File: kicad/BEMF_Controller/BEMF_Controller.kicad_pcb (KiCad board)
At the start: 2 copper layers, 201.8 x 175 mm, 228 parts, among them J1 HEADER4VALULOK, J2 HEADER6, J3 FUSE, J4 HEADER6, J5 Load, J7 Vin, Q1 C3M0280090D, Q11 C3M0280090D, Q2 C3M0280090D, Q3 C3M0280090D, Q4 C3M0280090D, Q5 C3M0280090D, Q6 C3M0280090D, Q7 C3M0280090D, Q9 C3M0280090D, U1 Raspberry Pi Pico, U10 OPA2376AIDR, U11 ADC108S022CIMTX/NOPB, U12 OPA2376AIDR, U13 INA181, U14 INA181, U15 INA181, U16 OPA2376AIDR, U18 ISO7760FQDWRQ1, U19 DGD2304, U2 INA181, U20 DGD2304, U21 DGD2304, U3 V_REG_78XX, U4 TC1240A, U5 DGD2304, U6 DGD2304, U7 DGD2304, U8 ISO7760FQDWRQ1, U9 ISO7760FQDWRQ1

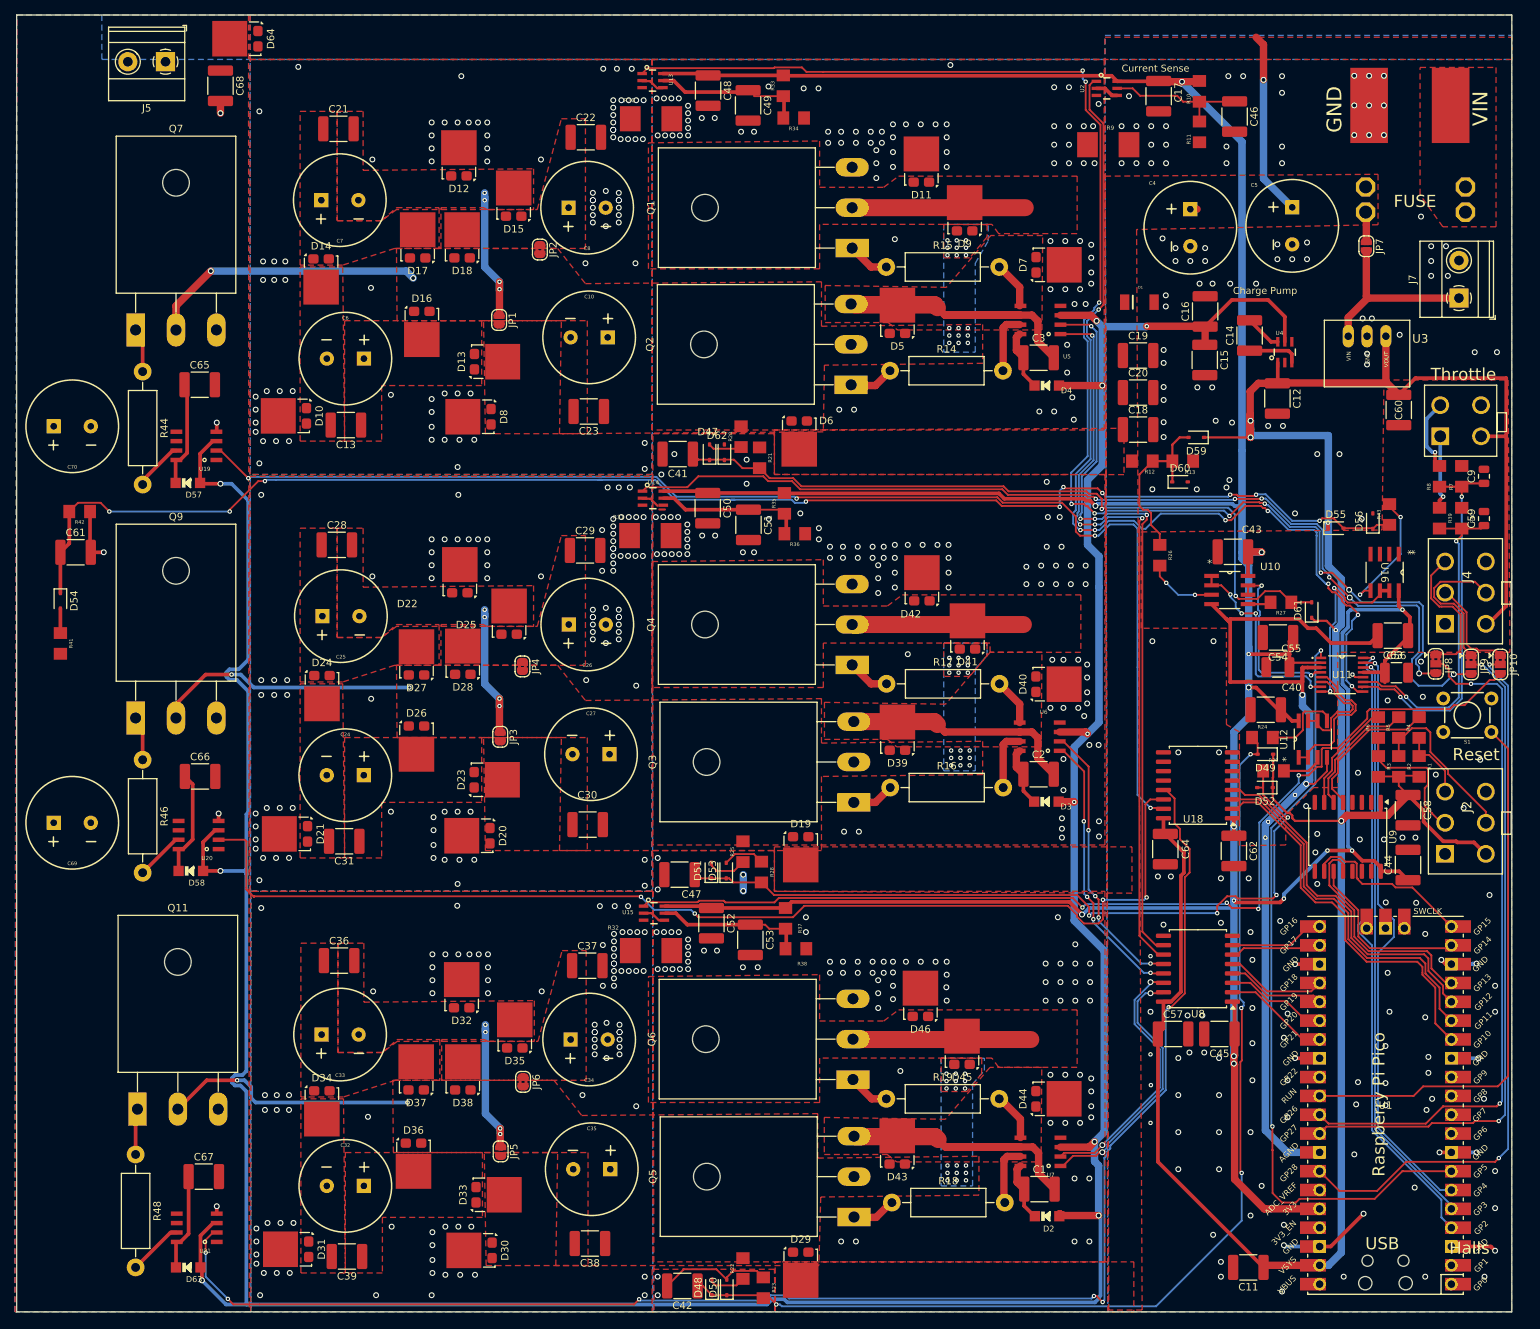
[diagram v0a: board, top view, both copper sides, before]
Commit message: Added analog Hall inputs and worked away lot of warnings.
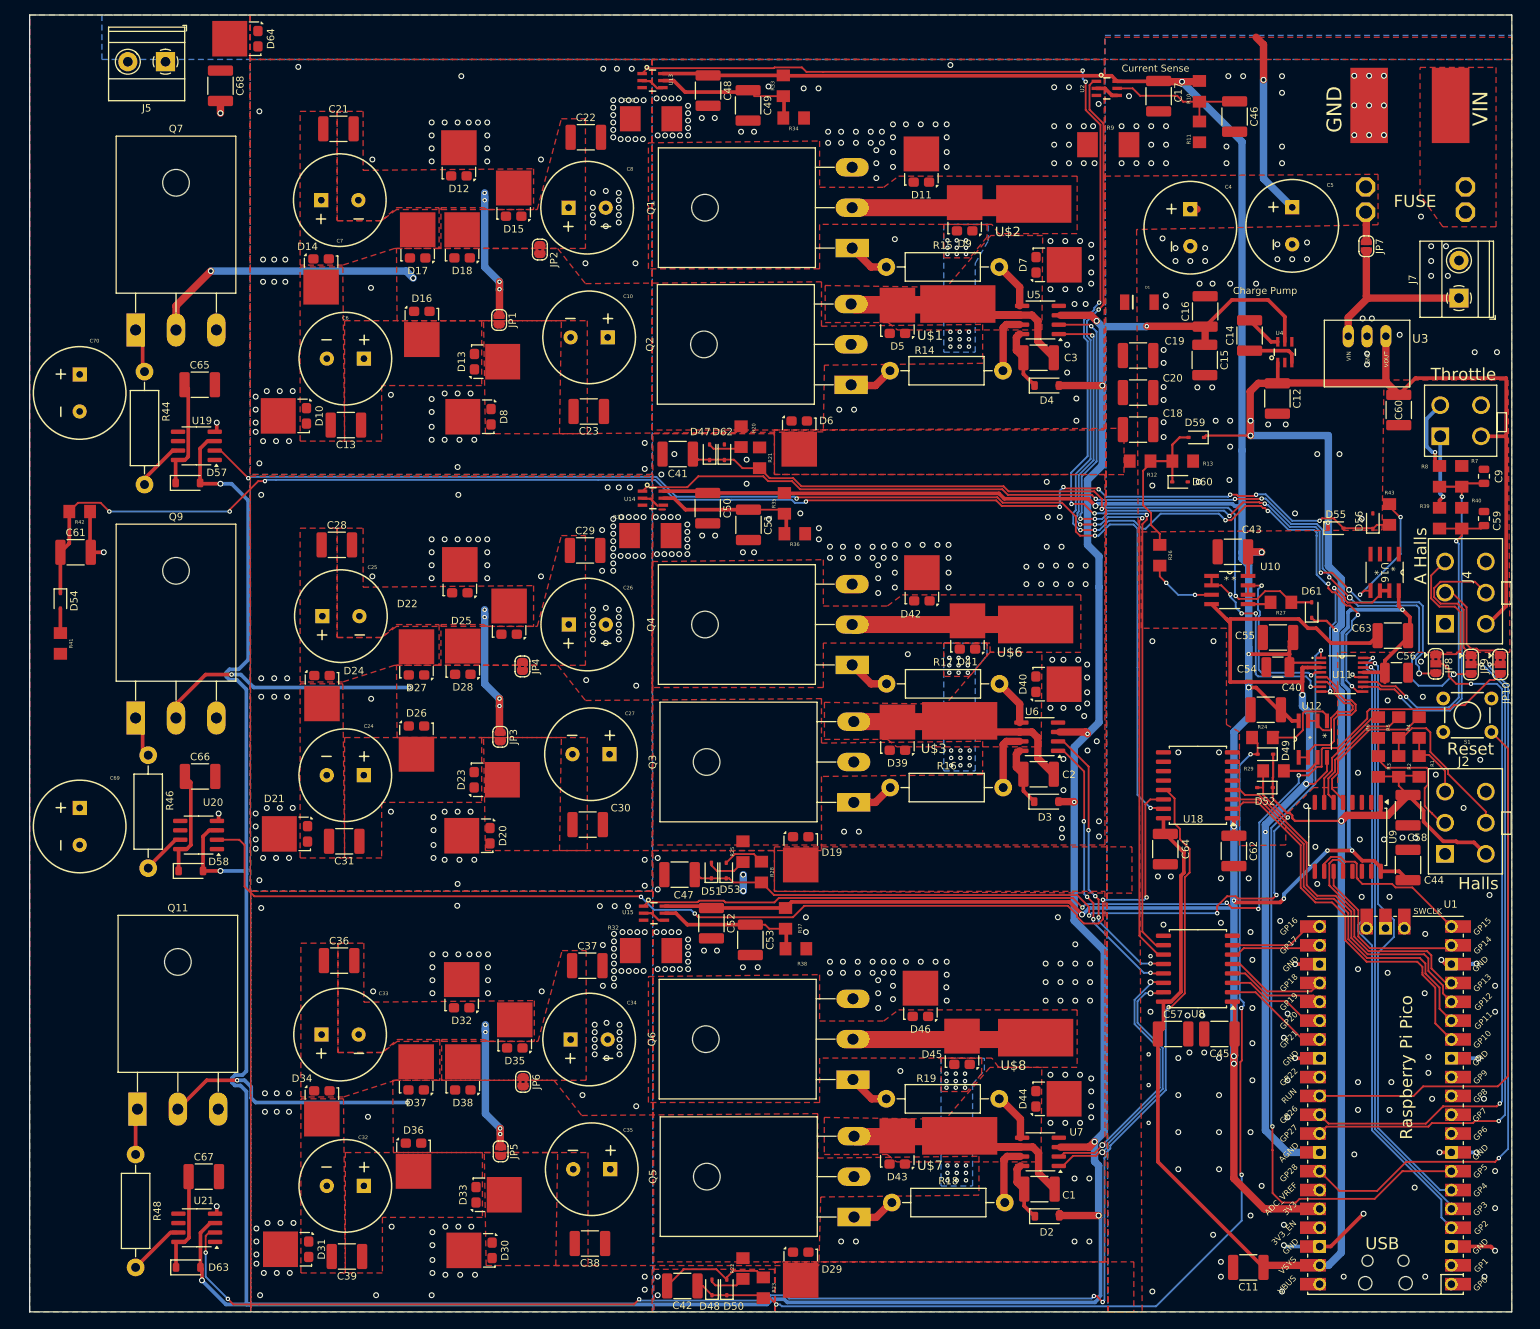
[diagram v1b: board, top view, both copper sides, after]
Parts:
- added U$1: PAD, main:PAD, F.Cu at (234.0, 92.8)
- added U$2: PAD, main:PAD, F.Cu at (244.2, 79.2)
- added U$3: PAD, main:PAD, F.Cu at (234.2, 149.0)
- added U$6: PAD, main:PAD, F.Cu at (244.5, 136.0)
- added U$7: PAD, main:PAD, F.Cu at (234.2, 205.0)
- added U$8: PAD, main:PAD, F.Cu at (244.5, 191.8)
- D2, D3, D4, D57, D58, D63: footprint main:SOD-123 -> Diode_SMD:D_SOD-123
- U19, U20, U21, U5, U6, U7: footprint main:SOIC8 -> Package_SO:SOIC-8_3.9x4.9mm_P1.27mm
- moved C70 4.61 mm to (115.5, 104.8), turned to 90 degrees
- moved C69 1.12 mm to (115.5, 163.2), turned to 90 degrees
- moved R46 0.97 mm to (124.8, 153.6)
- moved R12 0.30 mm to (258.6, 114.0)
- moved R44 0.25 mm to (124.2, 101.9)
- turned D2 to 0 degrees
- turned D3 to 0 degrees
- turned D4 to 0 degrees
- turned D57 to 0 degrees
- turned D58 to 0 degrees
- turned D63 to 0 degrees
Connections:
- C1 pad 1: Net-(U7-VB) -> Net-(D2-K)
- C2 pad 1: Net-(U6-VB) -> Net-(D3-K)
- C3 pad 1: Net-(U5-VB) -> Net-(D4-K)
- C65 pad 1: Net-(U19-VB) -> Net-(D57-K)
- C66 pad 1: Net-(U20-VB) -> Net-(D58-K)
- C67 pad 1: Net-(U21-VB) -> Net-(D63-K)
- U19 pad 8: Net-(U19-VB) -> Net-(D57-K)
- U20 pad 8: Net-(U20-VB) -> Net-(D58-K)
- U21 pad 8: Net-(U21-VB) -> Net-(D63-K)
- U5 pad 8: Net-(U5-VB) -> Net-(D4-K)
- U6 pad 8: Net-(U6-VB) -> Net-(D3-K)
- U7 pad 8: Net-(U7-VB) -> Net-(D2-K)
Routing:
- net Net-(D57-K): track 0.00 -> 14.8 mm
- net Net-(D58-K): track 0.00 -> 14.4 mm
- net Net-(U19-VB): track 14.3 -> 0.00 mm
- net Net-(U20-VB): track 14.3 -> 0.00 mm
- net Net-(D63-K): track 0.00 -> 13.6 mm
- net Net-(U21-VB): track 13.2 -> 0.00 mm
- net Net-(U7-VB): track 8.04 -> 0.00 mm
- net Net-(U6-VB): track 8.04 -> 0.00 mm
- net Net-(D3-K): track 0.00 -> 8.04 mm
- net Net-(D2-K): track 0.00 -> 8.04 mm
- net Net-(U5-VB): track 8.04 -> 0.00 mm
- net Net-(D4-K): track 0.00 -> 8.04 mm
- net 5V: track 364.0 -> 359.1 mm
- net 3.3V: track 527.7 -> 526.2 mm
- net /DCH_B_H: track 6.69 -> 5.76 mm
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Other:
- board size 201.8 x 175 mm -> 200 x 175 mm
- board text added: "A Halls"

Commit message: Simplification, high and low side driven together.
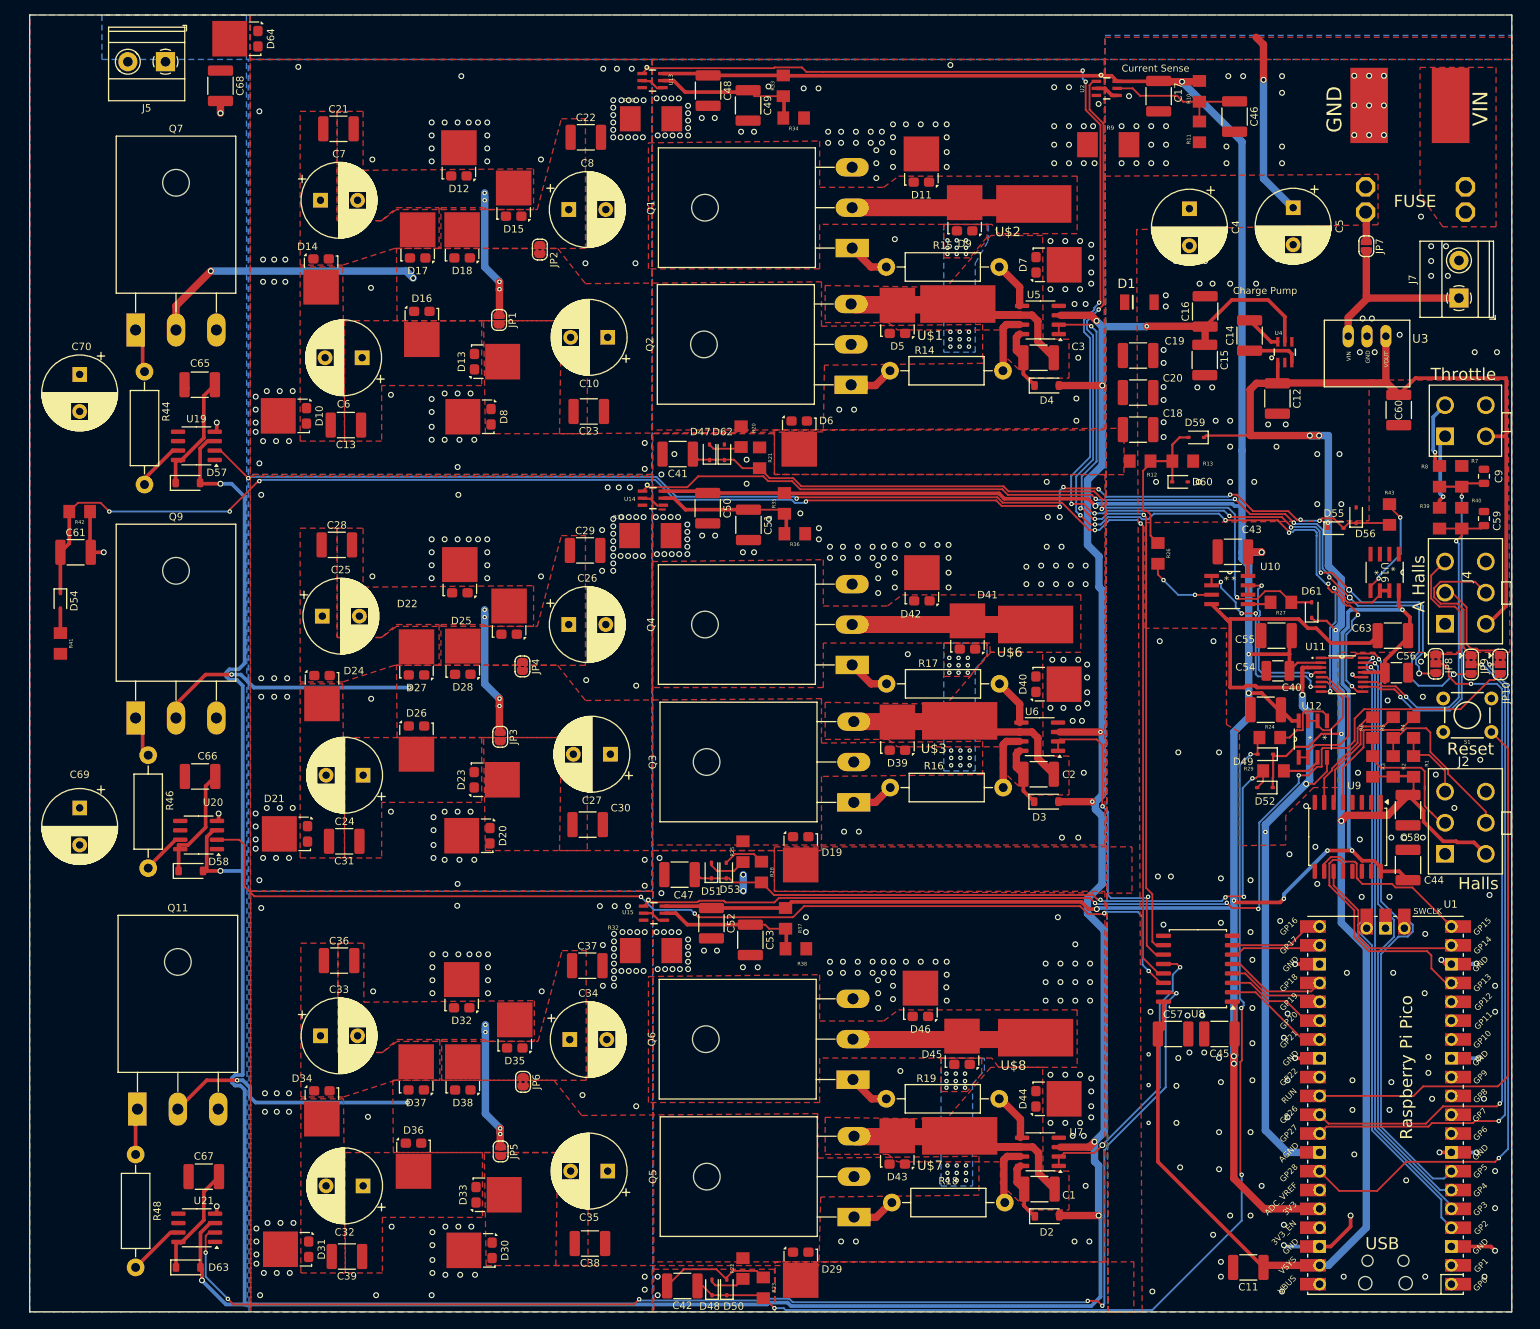
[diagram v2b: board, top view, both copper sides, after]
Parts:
- removed C62, C64: 1uF, Capacitor_SMD:C_1812_4532Metric
- removed U18: ISO7760FQDWRQ1, Package_SO:SOIC-16W_7.5x10.3mm_P1.27mm
- C10, C24, C25, C26, C27, C32, C33, C34, C35, C4, C5, C6, C69, C7, C70, C8: footprint main:CPOL-RADIAL-5MM-10MM -> Capacitor_THT:CP_Radial_D10.0mm_P5.00mm
- U$1: value PAD -> COIL_A+
- moved C33 2.65 mm to (148.0, 191.5), turned to 0 degrees
- moved C27 2.62 mm to (187.1, 153.5), turned to 180 degrees
- moved C34 2.62 mm to (181.6, 192.0), turned to 0 degrees
- moved C7 2.60 mm to (148.0, 78.8), turned to 0 degrees
- moved C4 2.57 mm to (265.2, 79.9), turned to -90 degrees
- moved C10 2.50 mm to (186.8, 97.2), turned to 180 degrees
- moved C25 2.50 mm to (148.2, 134.9), turned to 0 degrees
- moved C26 2.50 mm to (181.5, 136.0), turned to 0 degrees
- moved C69 2.50 mm to (115.5, 160.8), turned to -90 degrees
- moved C70 2.50 mm to (115.5, 102.2), turned to -90 degrees
- moved C8 2.49 mm to (181.5, 80.0), turned to 0 degrees
- moved C5 2.45 mm to (279.2, 79.8), turned to -90 degrees
- moved C24 2.41 mm to (153.8, 156.3), turned to 180 degrees
- moved C32 2.40 mm to (153.8, 211.8), turned to 180 degrees
- moved D56 2.39 mm to (287.8, 121.2)
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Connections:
- net /AH_O renamed /A_O
- net /AL_O renamed /B_O
- net /BH_O renamed /C_O
- U1 pad 14: /DA_O -> unconnected-(U1-GPIO10-Pad14)
- U1 pad 15: /DB_O -> unconnected-(U1-GPIO11-Pad15)
- U1 pad 16: /DC_O -> unconnected-(U1-GPIO12-Pad16)
- U1 pad 25: /BL_O -> /DA_O
- U1 pad 26: /CH_O -> /DB_O
- U1 pad 27: /CL_O -> /DC_O
- U1 pad 42: unconnected-(U1-GND-Pad42) -> GND
- U5 pad 1: /CTRL_AL -> /CTRL_A
- U5 pad 2: /CTRL_AH -> /CTRL_A
- U6 pad 1: /CTRL_BL -> /CTRL_B
- U6 pad 2: /CTRL_BH -> /CTRL_B
- U7 pad 1: /CTRL_CL -> /CTRL_C
- U7 pad 2: /CTRL_CH -> /CTRL_C
- U8 pad 10: /CTRL_AH -> /CTRL_A
- U8 pad 11: /CTRL_AL -> /CTRL_B
- U8 pad 12: /CTRL_BH -> /CTRL_C
- U8 pad 13: /CTRL_BL -> /CTRL_DA
- U8 pad 14: /CTRL_CH -> /CTRL_DB
- U8 pad 15: /CTRL_CL -> /CTRL_DC
- U8 pad 2: /CL_O -> /DC_O
- U8 pad 3: /CH_O -> /DB_O
- U8 pad 4: /BL_O -> /DA_O
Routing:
- net /CTRL_AH: track 100.8 -> 0.00 mm, vias 4 -> 0
- net /CTRL_AL: track 100.8 -> 0.00 mm, vias 4 -> 0
- net /CTRL_A: track 0.00 -> 100.5 mm, vias 0 -> 4
- net /CTRL_B: track 0.00 -> 43.3 mm, vias 0 -> 2
- net /DA_O: track 51.9 -> 13.4 mm
- net /CTRL_C: track 0.00 -> 38.4 mm, vias 0 -> 2
- net /CTRL_BH: track 37.9 -> 0.00 mm, vias 4 -> 0
- net /CTRL_BL: track 37.7 -> 0.00 mm, vias 4 -> 0
- net /DB_O: track 49.8 -> 13.9 mm
- net /CTRL_CH: track 35.6 -> 0.00 mm, vias 2 -> 0
- net /CTRL_CL: track 35.6 -> 0.00 mm, vias 2 -> 0
- net /DC_O: track 48.4 -> 14.4 mm
- net /CTRL_DC: track 206.9 -> 179.0 mm
- net /CTRL_DA: track 171.6 -> 192.6 mm
- net 5V: track 359.1 -> 343.0 mm, vias 5 -> 6
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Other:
- board text added: "DUTY"

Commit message: Fixed all warnings.
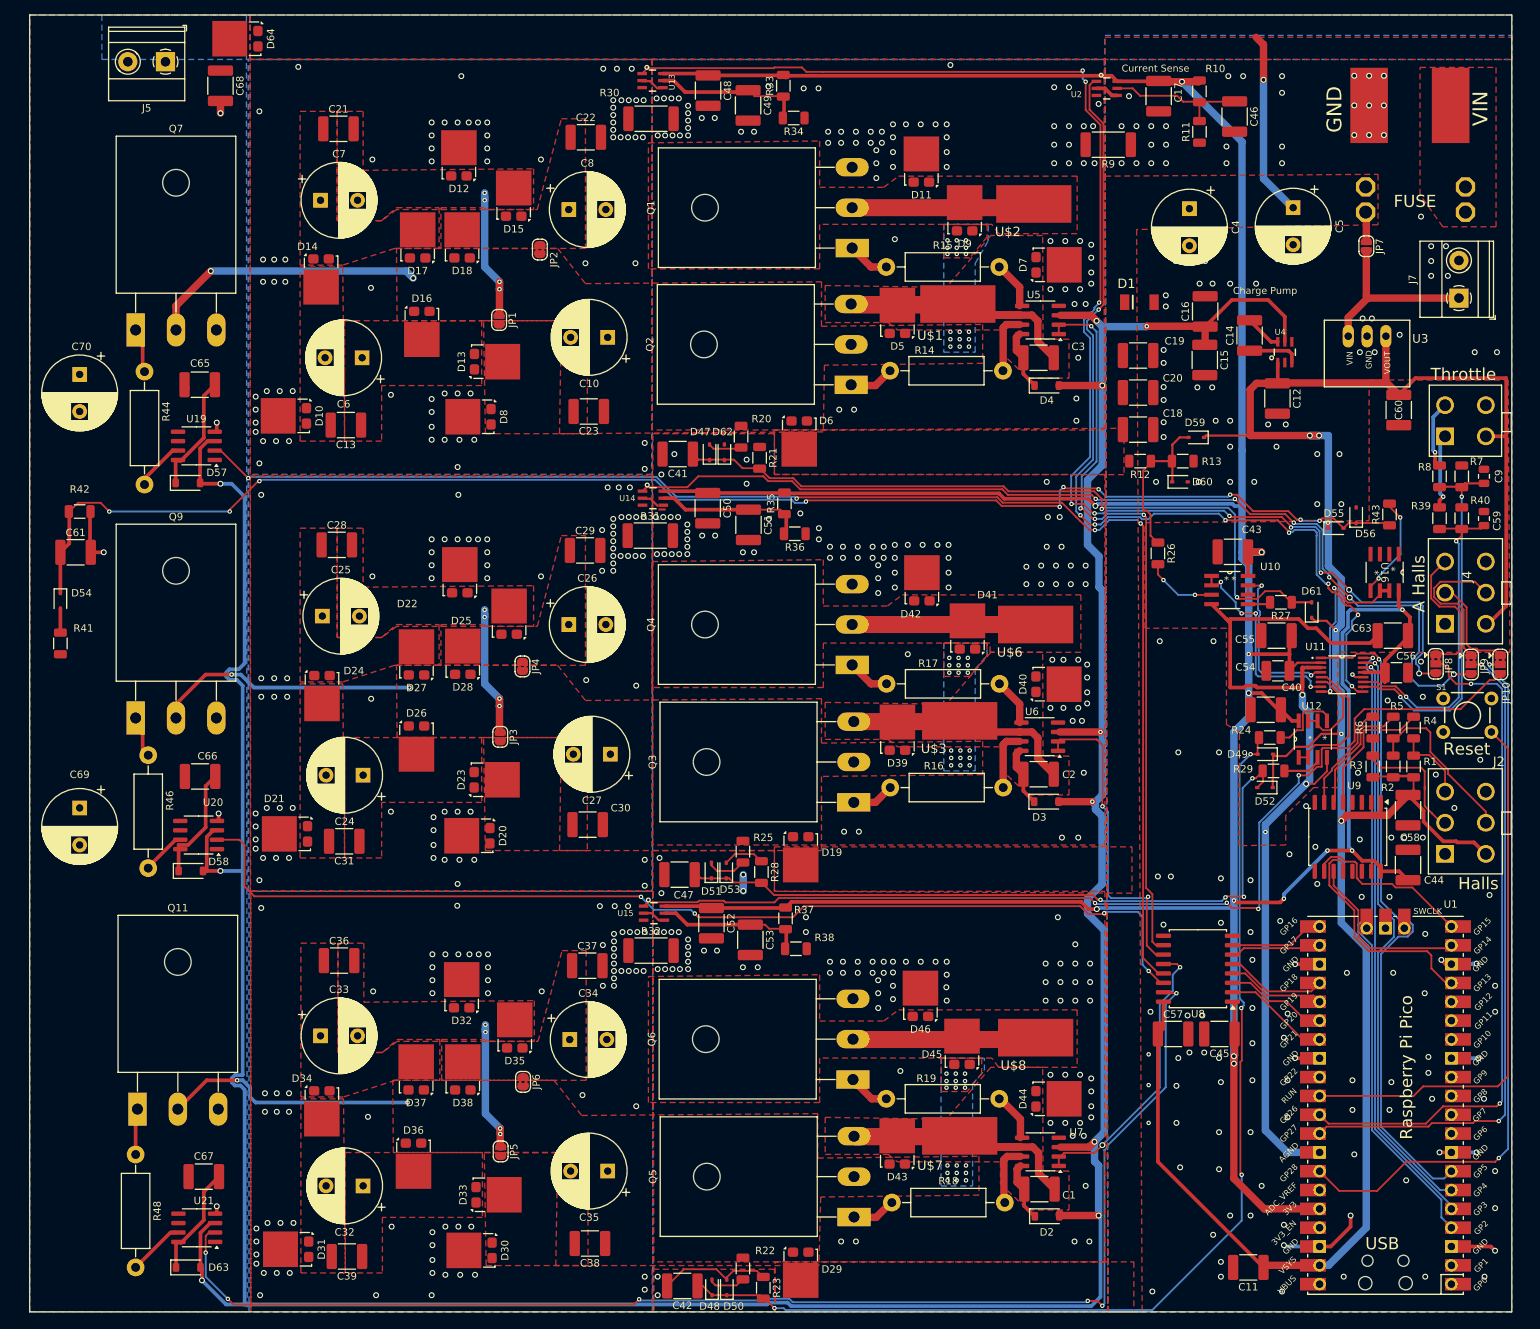
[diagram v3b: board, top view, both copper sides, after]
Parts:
- R1, R10, R11, R12, R13, R2, R20, R21, R22, R23, R24, R25, R26, R27, R28, R29, R3, R33, R34, R35, R36, R37, R38, R39, R4, R40, R41, R42, R43, R5, R6, R7, R8: footprint main:1206 -> Resistor_SMD:R_1206_3216Metric
- R30, R31, R32, R9: footprint main:R2512 -> Resistor_SMD:R_2512_6332Metric_Pad1.40x3.35mm_HandSolder
